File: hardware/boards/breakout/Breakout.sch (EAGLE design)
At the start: 4 parts

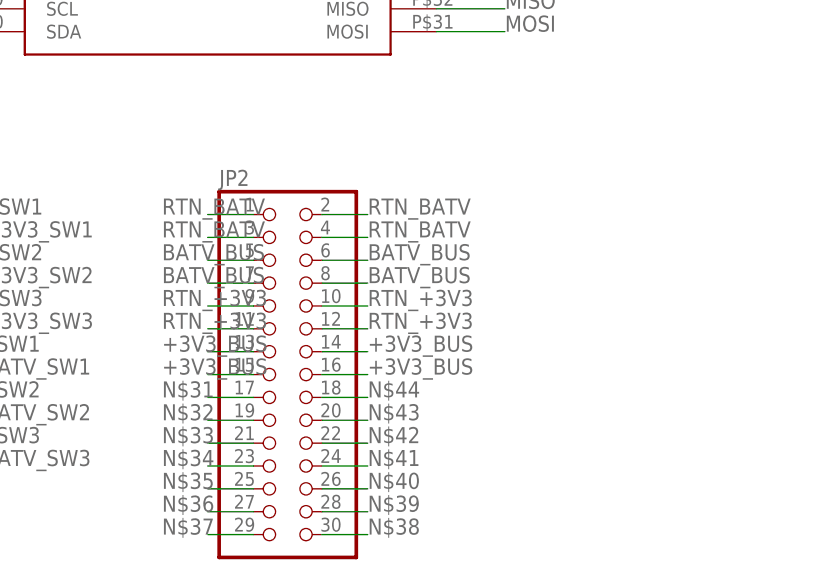
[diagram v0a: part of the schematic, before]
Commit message: completed routing breakout, need to tidy
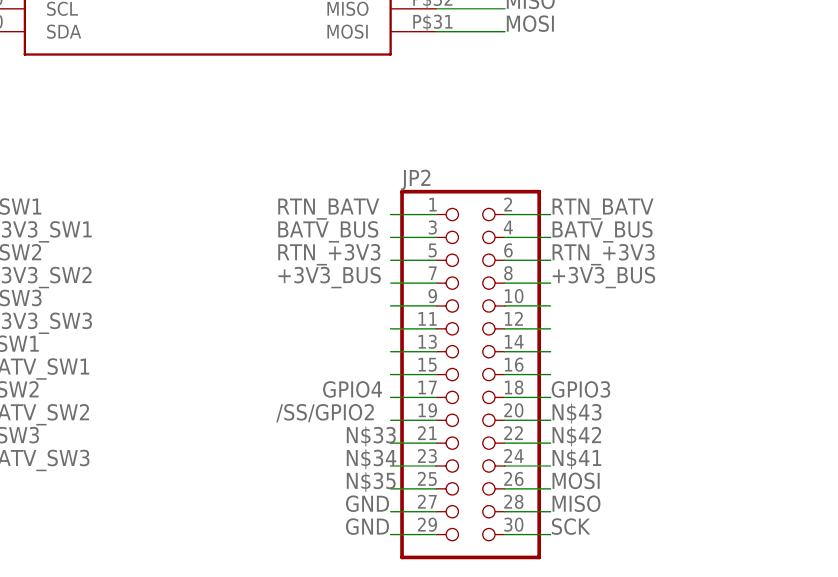
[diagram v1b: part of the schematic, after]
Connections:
- removed net N$31: JP2.17
- removed net N$32: JP2.19
- removed net N$36: JP2.27
- removed net N$37: JP2.29
- removed net N$38: JP2.30
- removed net N$39: JP2.28
- removed net N$40: JP2.26
- removed net N$44: JP2.18
- net +3V3_BUS: now also JP2.7, JP2.8; no longer JP2.13, JP2.14, JP2.15, JP2.16
- net /SS/GPIO2: now also JP2.19
- net BATV_BUS: now also JP2.3, JP2.4; no longer JP2.5, JP2.6, JP2.7, JP2.8
- net GND: now also JP2.27, JP2.29
- net GPIO10: now also JP2.11
- net GPIO11: now also JP2.10
- net GPIO12: now also JP2.9
- net GPIO3: now also JP2.18
- net GPIO4: now also JP2.17
- net GPIO5: now also JP2.16
- net GPIO6: now also JP2.15
- net GPIO7: now also JP2.14
- net GPIO8: now also JP2.13
- net GPIO9: now also JP2.12
- net MISO: now also JP2.28
- net MOSI: now also JP2.26
- net RTN_+3V3: now also JP2.5, JP2.6; no longer JP2.10, JP2.11, JP2.12, JP2.9
- net RTN_BATV: no longer JP2.3, JP2.4
- net SCK: now also JP2.30
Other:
- moved on the sheet: JP2
